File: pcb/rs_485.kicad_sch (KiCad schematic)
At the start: 8 parts, among them U10 MAX13487E

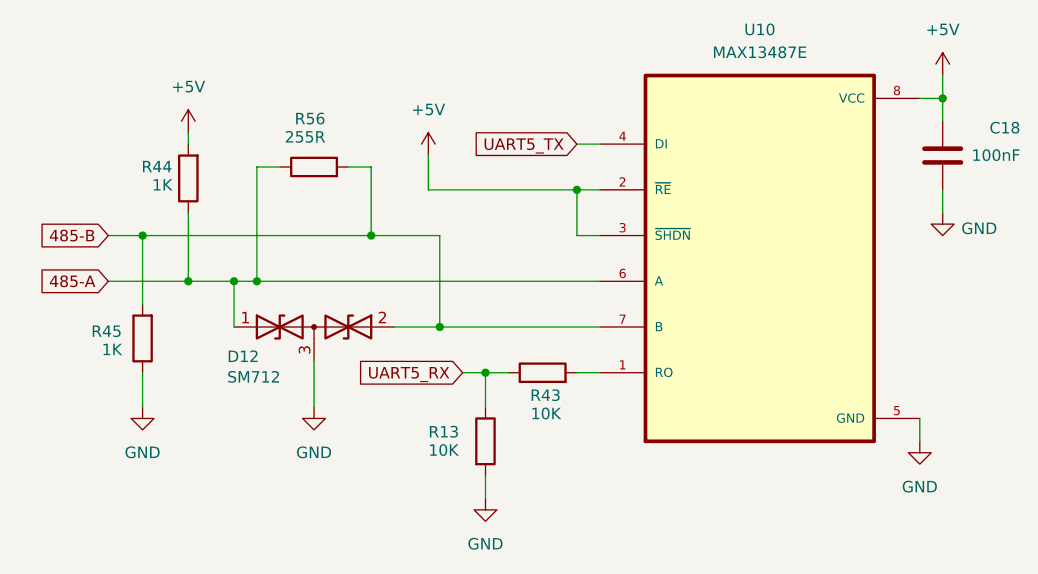
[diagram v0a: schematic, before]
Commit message: Marked a resistor as "Do not mount" to improve RS-485 reception.
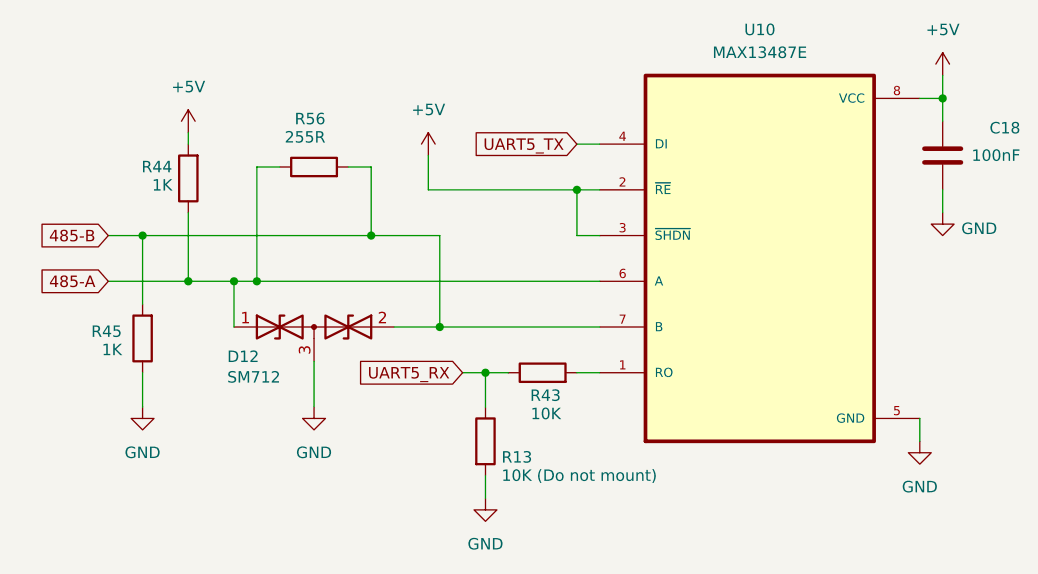
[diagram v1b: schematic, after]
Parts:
- R13: value 10K -> 10K (Do not mount)
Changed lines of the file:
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@@
 		(dnp no)
 		(property "Reference" "R13"
-			(at 138.43 103.124 0)
+			(at 146.558 105.918 0)
 			(effects
 				(font
@@
 			)
 		)
-		(property "Value" "10K"
-			(at 138.43 105.156 0)
+		(property "Value" "10K (Do not mount)"
+			(at 146.558 107.95 0)
 			(effects
 				(font
